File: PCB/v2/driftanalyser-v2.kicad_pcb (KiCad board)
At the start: 4 copper layers, 110 x 75 mm, 101 parts, among them J1 XT60PW-M, J11 LED1, J12 LED2, J13 LED3, J14 LED4, J15 LED5, J16 LED6, J2 USB-C 16P, J3 UART0, J4 EXT, J5 microSD, J6 OBD, SW1 EN, SW2 BOOT, U1 ESP32-S3-WROOM-1-N16R2, U2 BTS7002-1EPP, U3 AP63200WU-7, U4 AP7361C-33E, U5 LSM6DS3TR-C, U6 USBLC6-2SC6, U7 74HCT245PW, U8 TJA1051T/3, U9 TJA1027T/20

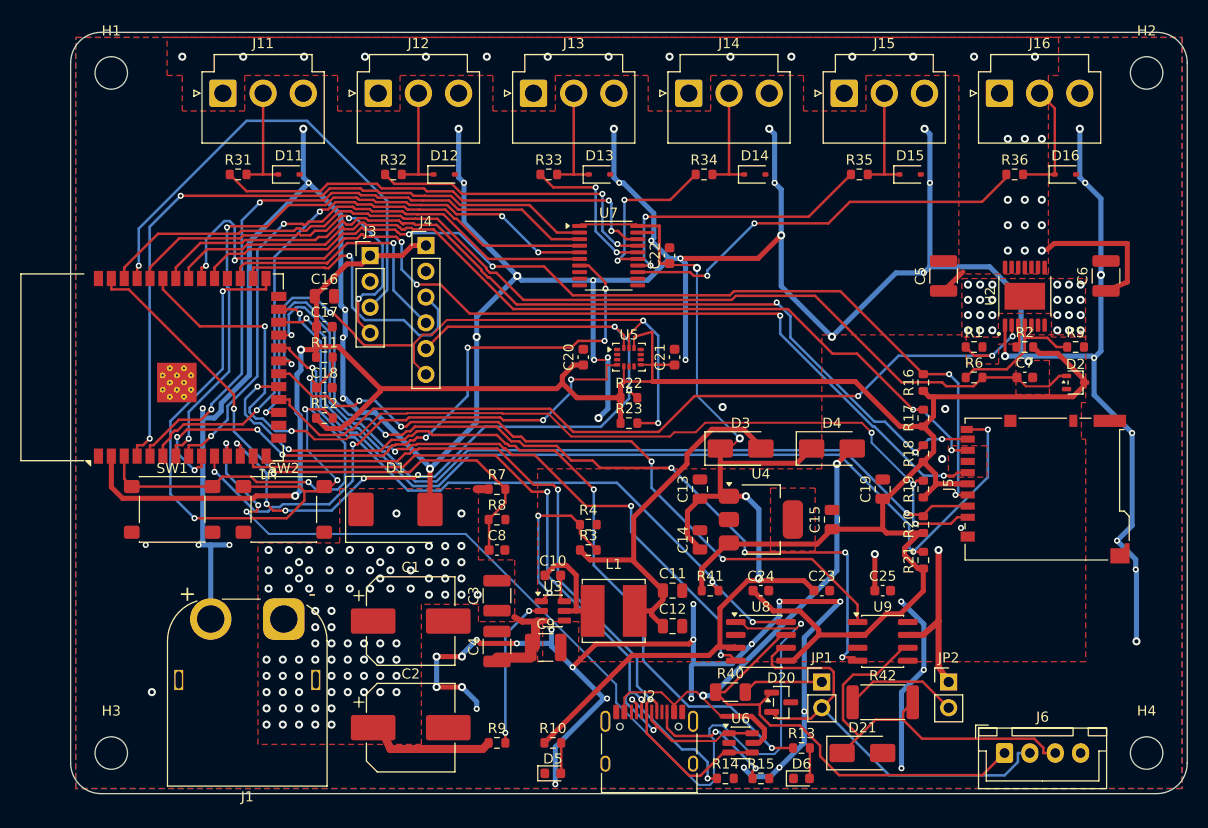
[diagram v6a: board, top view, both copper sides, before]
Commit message: pcb v2: silk, gerbers, jlc bom + cpl, 3d
Claude-Session: https://claude.ai/code/session_015oqRiQH5gUcw5a6jvR5Zdk
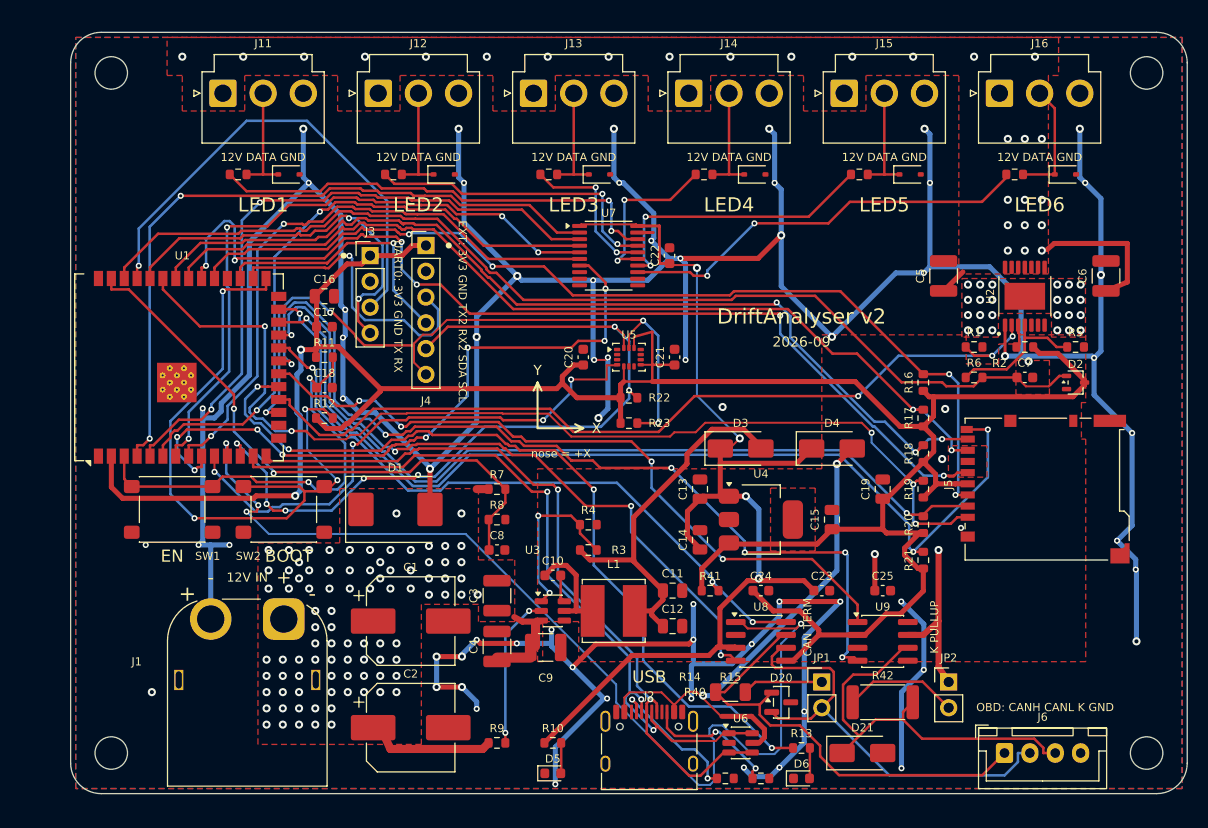
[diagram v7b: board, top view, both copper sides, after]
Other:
- board text added: "+"
- board text added: "-"
- board text added: "12V DATA GND"
- board text added: "12V IN"
- board text added: "2026-09"
- board text added: "BOOT"
- board text added: "CAN TERM"
- board text added: "DriftAnalyser v2"
- board text added: "EN"
- board text added: "EXT: 3V3 GND TX2 RX2 SDA SCL"
- board text added: "K PULLUP"
- board text added: "LED1"
- board text added: "LED2"
- board text added: "LED3"
- board text added: "LED4"
- board text added: "LED5"
- board text added: "LED6"
- board text added: "OBD: CANH CANL K GND"
- board text added: "UART0: 3V3 GND TX RX"
- board text added: "USB"
- board text added: "X"
- board text added: "Y"
- board text added: "nose = +X"

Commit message: pcb v2: xt60 pin 2 is +, not pin 1
Claude-Session: https://claude.ai/code/session_015oqRiQH5gUcw5a6jvR5Zdk
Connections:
- J1 pad 1: VBAT -> GND
- J1 pad 2: GND -> VBAT
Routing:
- net GND: track 458.3 -> 451.0 mm
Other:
- board text added: "CANH"
- board text added: "CANL"
- board text added: "GND"
- board text added: "K"
- board text added: "OBD"
- board text removed: "OBD: CANH CANL K GND"
